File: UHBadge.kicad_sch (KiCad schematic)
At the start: 0 parts

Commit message: Added the RP2350. Added the USB-C. Added the battery. Started working on the recharge system.
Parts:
- added BT1: Battery, symbol Device:Battery
- added C1, C16, C17, C2, C3, C5: 4.7uF, symbol Device:C
- added C10, C11, C12, C13, C14, C15, C4, C6, C7, C8, C9: 100nF, symbol Device:C
- added C18: 10uF, symbol Device:C
- added D1, D2, D3: LED, symbol Device:LED
- added L1: 3.3u, symbol Device:L
- added P1: USB_C_Plug_USB2.0, symbol Connector:USB_C_Plug_USB2.0
- added R1: 33Ω, symbol Device:R
- added R2, R3: 27Ω, symbol Device:R
- added R4: 5.1kΩ, symbol Device:R
- added R5, R6, R7: 470Ω, symbol Device:R
- added U1: RP2350A, Package_DFN_QFN:QFN-60-1EP_7x7mm_P0.4mm_EP3.4x3.4mm, symbol MCU_RaspberryPi:RP2350A
- added U2: MCP73871, Package_DFN_QFN:QFN-20-1EP_4x4mm_P0.5mm_EP2.5x2.5mm, symbol Battery_Management:MCP73871
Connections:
- new net: R7.1, U2.7 (STAT2)
- new net: D3.1 (K), R7.2
- new net: C1.1, R1.2, U1.46 (VREG_AVDD)
- new net: R6.1, U2.8 (STAT1/~{LBO})
- new net: D2.1 (K), R6.2
- new net: P1.A5 (CC), R4.1
- new net: R2.2, U1.51 (USB_DM)
- new net: L1.2, U1.48 (VREG_LX)
- new net: R5.1, U2.6 (~{PG})
- new net: R3.2, U1.52 (USB_DP)
- new net: D1.1 (K), R5.2
- new net +1V1: C3.1, C4.1, C5.1, C6.1, L1.1, U1.23 (DVDD), U1.39 (DVDD), U1.50 (VREG_FB), U1.6 (DVDD)
- new net +3V3: BT1.1 (+), C10.1, C11.1, C12.1, C13.1, C14.1, C15.1, C16.2, C17.2, C2.1, C7.1, C8.1, C9.1, R1.1, U1.1 (IOVDD), U1.11 (IOVDD), U1.20 (IOVDD), U1.30 (IOVDD), U1.38 (IOVDD), U1.44 (ADC_AVDD), U1.45 (IOVDD), U1.49 (VREG_VIN), U1.53 (USB_OTP_VDD), U1.54 (QSPI_IOVDD), U2.1 (OUT), U2.14 (V_{BAT}), U2.15 (V_{BAT}), U2.16 (V_{BAT_SENSE}), U2.20 (OUT)
- new net -BATT: BT1.2 (-), C1.2, C10.2, C11.2, C12.2, C13.2, C14.2, C15.2, C16.1, C17.1, C18.2, C2.2, C3.2, C4.2, C5.2, C6.2, C7.2, C8.2, C9.2, P1.A1 (GND), P1.A12 (GND), P1.B1 (GND), P1.B12 (GND), P1.SH (SHIELD), R4.2, U1.47 (VREG_PGND), U1.61 (GND), U2.10 (V_{SS}), U2.11 (V_{SS}), U2.21 (V_{SS}), U2.3 (SEL), U2.9 (~{TE})
- new net USB_C_D+: P1.A6 (D+), R3.1
- new net USB_C_D-: P1.A7 (D-), R2.1
- new net VDD: C18.1, D1.2 (A), D2.2 (A), D3.2 (A), P1.A4 (VBUS), P1.A9 (VBUS), P1.B4 (VBUS), P1.B9 (VBUS), U2.17 (CE), U2.18 (IN), U2.19 (IN), U2.2 (VPCC)
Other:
- note added: "BATTERY"
- note added: "MCP73871"
- note added: "RP2350 Decoupling Capacitors - Set 1"
- note added: "RP2350 Decoupling Capacitors - Set 2"
- note added: "USB C"

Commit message: Added the flash, fixed the RP2350 main connections.
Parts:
- added C19: 100nF, symbol Device:C
- added C20, C21: 15pF, symbol Device:C
- added J1: Conn_01x03_MountingPin, symbol Connector_Generic_MountingPin:Conn_01x03_MountingPin
- added R10, R11, R9: 1kΩ, symbol Device:R
- added R8: 0Ω, symbol Device:R
- added SW1: Boot, symbol Switch:SW_Push
- added SW2: Run, symbol Switch:SW_Push
- added U3: W25Q128JVS, Package_SO:SOIC-8_5.3x5.3mm_P1.27mm, symbol Memory_Flash:W25Q128JVS
- added Y1: 12MHz, symbol Device:Crystal
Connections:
- net +3V3: now also C19.1, U3.8 (VCC)
- net -BATT: now also C19.2, C20.2, C21.1, J1.2 (Pin_2), J1.MP (MountPin), R11.2, SW1.1, U3.4 (GND)
- net XIN: now reaches U1.21 (XIN)
- net XIN: now also C21.2, Y1.1
- net XOUT: now reaches U1.22 (XOUT)
- net XOUT: now also R10.2
- net SWCLK: now reaches U1.24 (SWCLK)
- net SWCLK: now also J1.1 (Pin_1)
- net SWDIO: now reaches U1.25 (SWDIO)
- net SWDIO: now also J1.3 (Pin_3)
- net RUN: now reaches U1.26 (RUN)
- net RUN: now also SW2.1
- net QSPI_SD3: now reaches U1.55 (QSPI_SD3)
- net QSPI_SD3: now also U3.7 (~{HOLD}/~{RESET}/IO_{3})
- net QSPI_SCLK: now reaches U1.56 (QSPI_SCLK)
- net QSPI_SCLK: now also U3.6 (CLK)
- net QSPI_SD0: now reaches U1.57 (QSPI_SD0)
- net QSPI_SD0: now also U3.5 (DI/IO_{0})
- net QSPI_SD2: now reaches U1.58 (QSPI_SD2)
- net QSPI_SD2: now also U3.3 (~{WP}/IO_{2})
- net QSPI_SD1: now reaches U1.59 (QSPI_SD1)
- net QSPI_SD1: now also U3.2 (DO/IO_{1})
- net QSPI_SS: now reaches U1.60 (~{QSPI_SS})
- net QSPI_SS: now also R8.2, R9.2
- new net: C20.1, R10.1, Y1.2
- new net: R9.1, SW1.2
- new net: R8.1, U3.1 (~{CS})
- new net: R11.1, SW2.2
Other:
- note added: "Battery Recharger"
- note added: "Boot"
- note added: "Crystal"
- note added: "Debug Pins"
- note added: "Flash"
- note added: "Run"
- note removed: "MCP73871"
- moved on the sheet: BT1, C1, C10, C11, C12, C13, C14, C15, C16, C17, C18, C2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

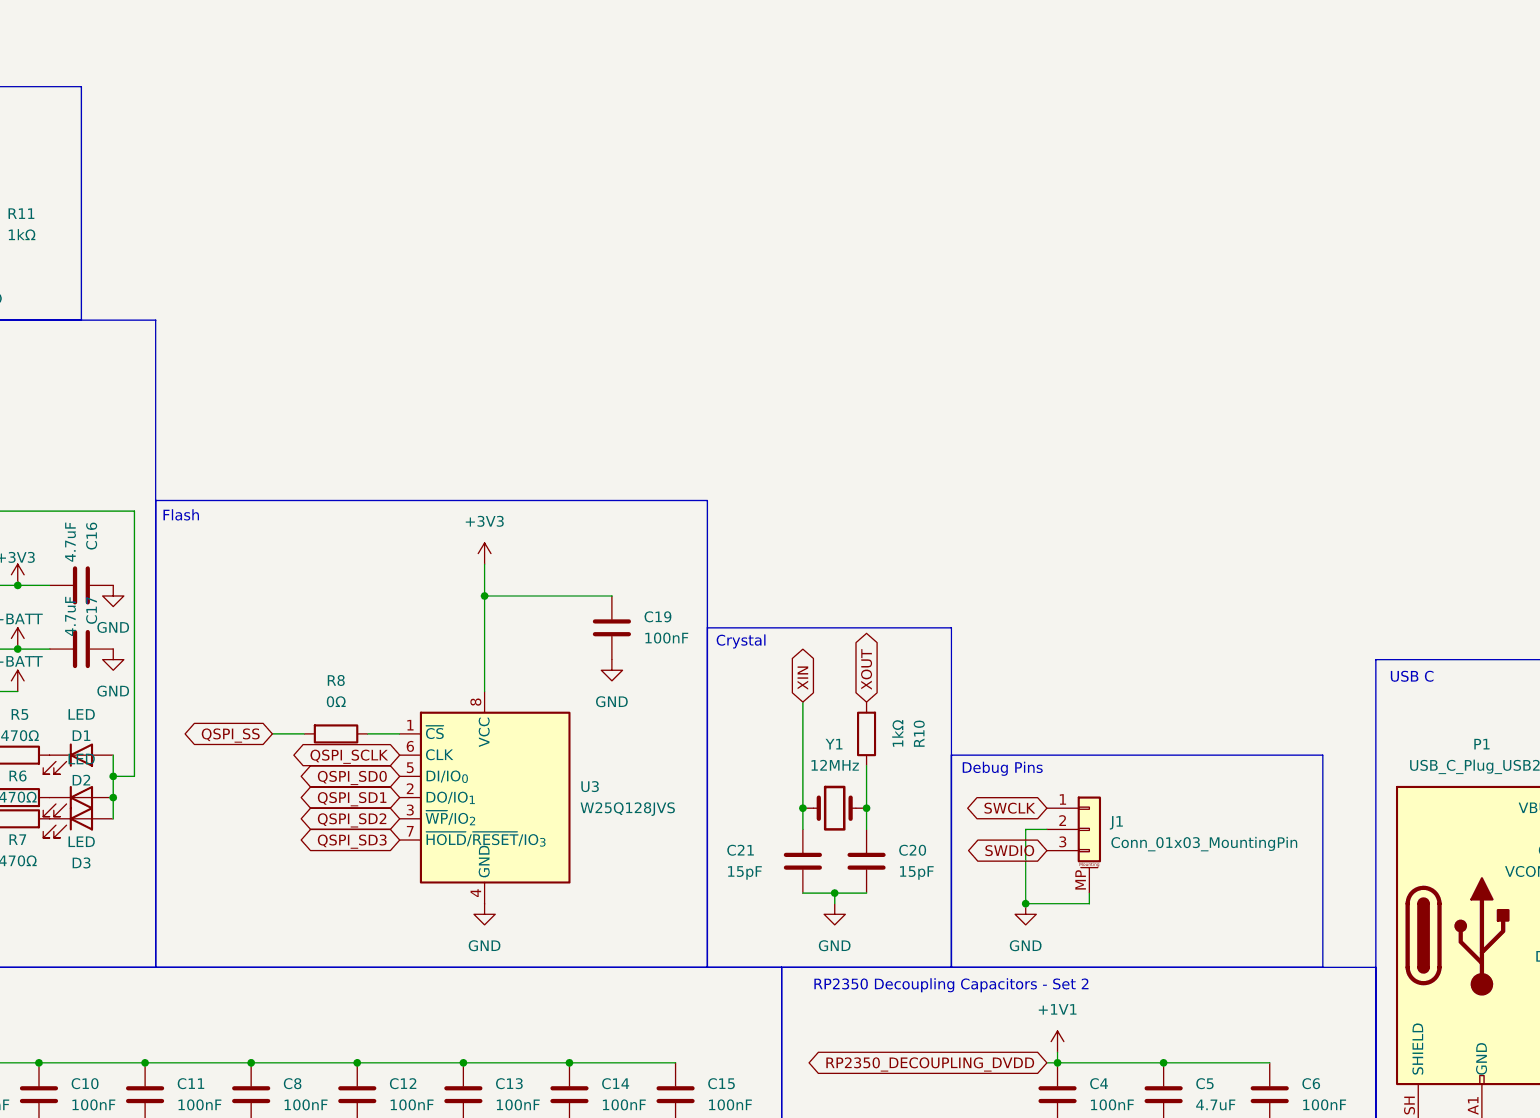
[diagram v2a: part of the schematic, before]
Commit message: Added esd protection.
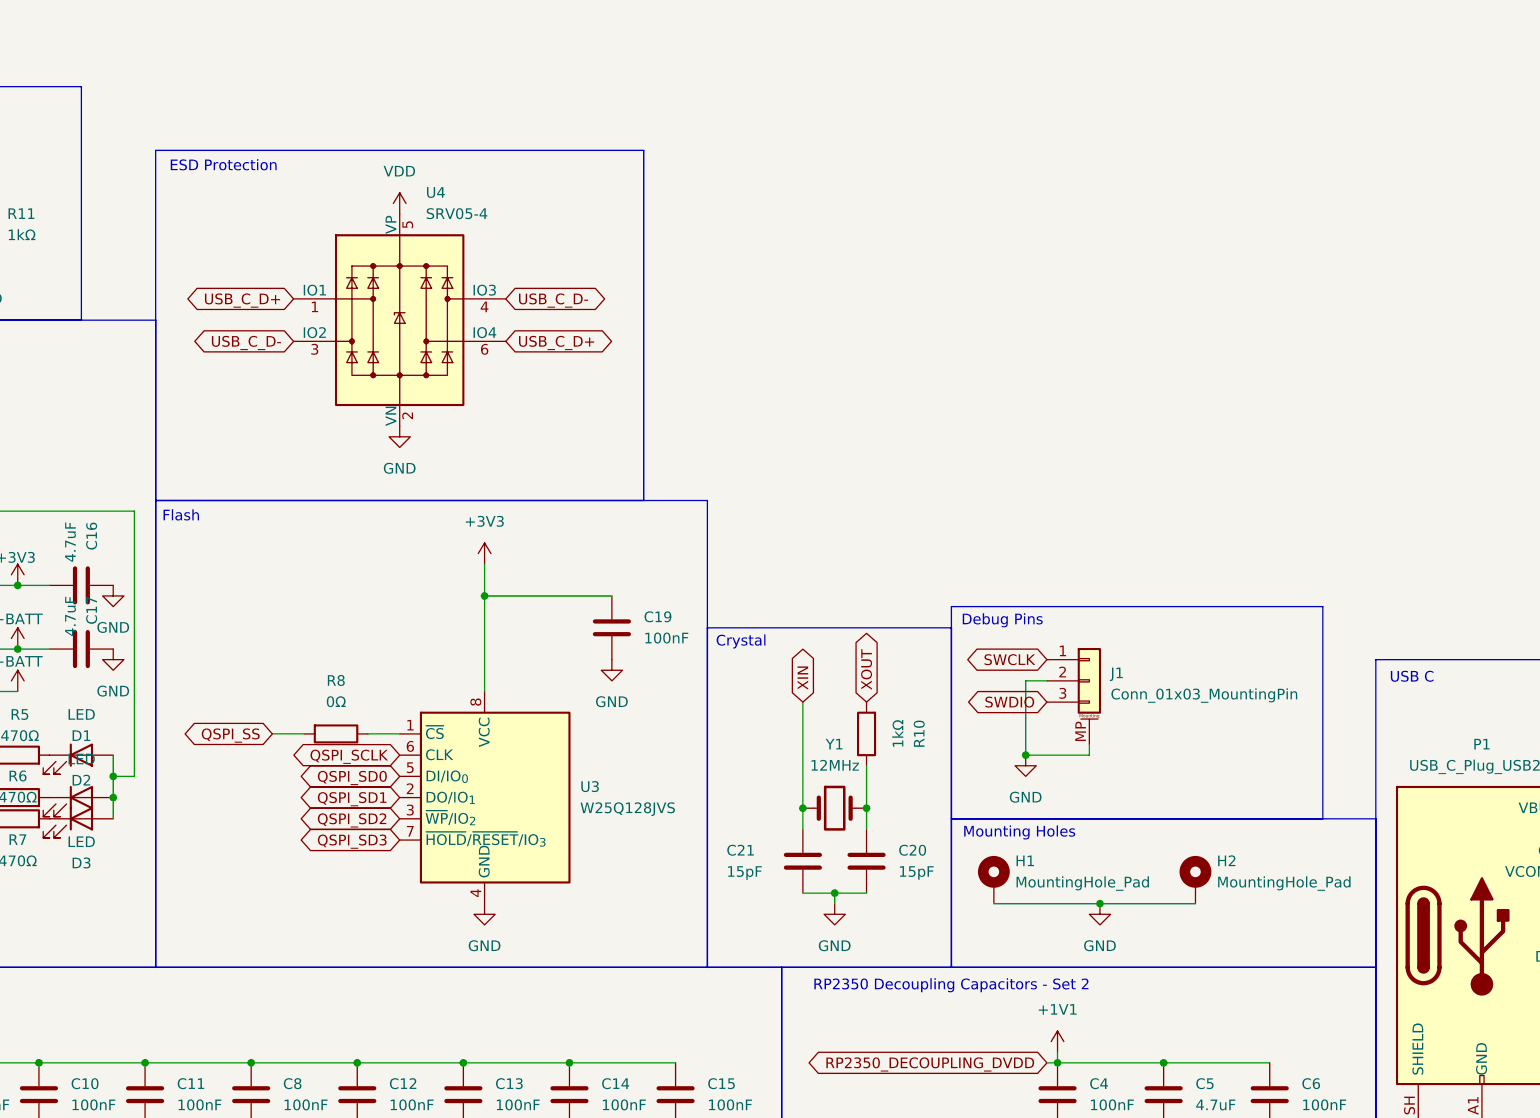
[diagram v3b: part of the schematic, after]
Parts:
- added H1, H2: MountingHole_Pad, symbol Mechanical:MountingHole_Pad
- added U4: SRV05-4, Package_TO_SOT_SMD:SOT-23-6, symbol Power_Protection:SRV05-4
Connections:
- net -BATT: now also H1.1, H2.1, U4.2 (VN)
- net USB_C_D+: now also U4.1 (IO1), U4.6 (IO4)
- net USB_C_D-: now also U4.3 (IO2), U4.4 (IO3)
- net VDD: now also U4.5 (VP)
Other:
- note added: "ESD Protection"
- note added: "Mounting Holes"
- moved on the sheet: J1

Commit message: Added the e-ink display.
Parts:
- added C22: 33pF, symbol Device:C
- added C23: 0.1uF, symbol Device:C
- added C24, C25, C26, C27, C28, C29, C30, C31, C32, C33: 1uF, symbol Device:C
- added C34, C35: 4.7uF, symbol Device:C
- added D4: LED, symbol Device:LED
- added D5, D6, D7: MBR0530, Diode_SMD:D_SOD-123, symbol Diode:MBR0530
- added L2: NFC Antenna, symbol Device:L
- added L3: 47uH 500mA, symbol Device:L
- added Q1: Si1308EDL, Package_TO_SOT_SMD:SOT-323_SC-70, symbol Transistor_FET:Si1308EDL
- added R12, R13, R14: 10kΩ, symbol Device:R
- added R15: 47Ω, symbol Device:R
- added R16: 1MΩ, symbol Device:R
- added R17: 2.2Ω, symbol Device:R
- added U5: Conn, Connector_FFC-FPC:Jushuo_AFC07-S24FCA-00_1x24-1MP_P0.50_Horizontal, symbol inkbadge:EINK-2.9inch
- added U6: ST25DV64K-JFR6D3, Package_DFN_QFN:ST_UFDFPN-12-1EP_3x3mm_P0.5mm_EP1.4x2.55mm, symbol RF_NFC:ST25DV64K-JFR6D3
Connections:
- net +3V3: now also C23.2, C31.2, C34.1, L3.1, R12.1, R13.1, R14.1, U5.10 (VDDIO), U5.9 (VCI), U6.10 (VDCG), U6.12 (VCC)
- net -BATT: now also C23.1, C24.1, C25.1, C26.1, C27.1, C28.1, C29.1, C30.1, C31.1, C32.1, C33.1, C34.2, D5.1 (K), R15.2, R16.1, R17.1, U5.17 (BS1), U5.8 (VSS), U5.MP (SHIELD), U6.6 (VSS)
- net NFC_SDA: now reaches U1.14 (GPIO10)
- net NFC_SDA: now also R13.2, U6.7 (SDA)
- net NFC_SCL: now reaches U1.15 (GPIO11)
- net NFC_SCL: now also R12.2, U6.8 (SCL)
- net NFC_GPO: now reaches U1.16 (GPIO12)
- net NFC_GPO: now also R14.2, U6.11 (GPO)
- net E-INK_BUSY: now reaches U1.17 (GPIO13)
- net E-INK_BUSY: now also U5.16 (BUSY)
- net E-INK_RST: now reaches U1.18 (GPIO14)
- net E-INK_RST: now also U5.15 (~{RST})
- net E-INK_D/C: now reaches U1.19 (GPIO15)
- net E-INK_D/C: now also U5.14 (~{D/C})
- net E-INK_CS: now reaches U1.27 (GPIO16)
- net E-INK_CS: now also U5.13 (~{CS})
- net E-INK_SCL: now reaches U1.28 (GPIO17)
- net E-INK_SCL: now also U5.12 (SCL)
- net E-INK_SDA: now reaches U1.29 (GPIO18)
- net E-INK_SDA: now also U5.11 (SDA)
- new net: C35.1, D5.2 (A), D6.1 (K)
- new net: C29.2, U5.7 (VDD)
- new net: C26.2, U5.3 (VSL)
- new net: C22.1, L2.1, U6.4 (AC0)
- new net: C22.2, L2.2, U6.5 (AC1)
- new net: D4.1 (K), R15.1
- new net: C35.2, D7.2 (A), L3.2, Q1.3 (D)
- new net: C25.2, U5.1 (NC)
- new net: D4.2 (A), U6.3 (V_EH)
- new net: C33.2, U5.20 (VSH2)
- new net: C32.2, U5.21 (VGL/NC)
- new net: C27.2, U5.5 (VSH1)
- new net: C30.2, U5.6 (VPP)
- new net E-INK_GDR: Q1.1 (G), R16.2, U5.23 (GDR)
- new net E-INK_RESE: Q1.2 (S), R17.2, U5.22 (RESE)
- new net E-INK_VGH: C28.2, D7.1 (K), U5.4 (VGH)
- new net E-INK_VGL: C24.2, D6.2 (A), U5.2 (VGL)
- no-connect marks 0 -> 4
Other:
- note added: "E-Ink Display"
- note added: "NFC"
- moved on the sheet: C20, C21, C4, C5, C6, H1, H2, J1, P1, R10, R11, R4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
